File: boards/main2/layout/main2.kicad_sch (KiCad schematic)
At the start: 25 parts, among them IC1 STM32H725RGV6

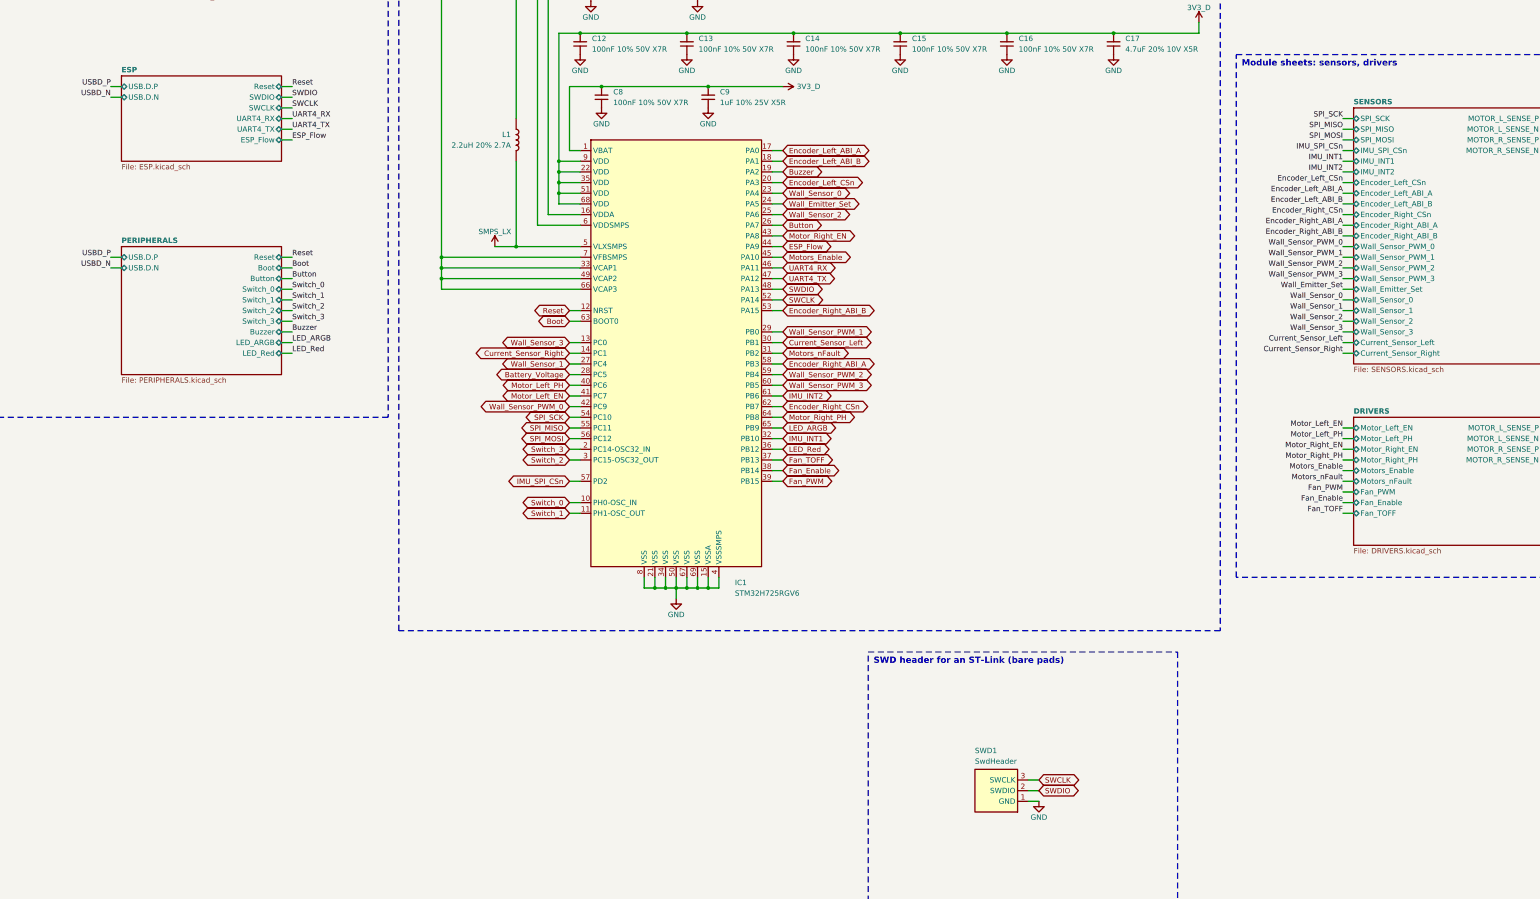
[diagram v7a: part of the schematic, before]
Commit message: 🚧 Swap main2's USB and ESP32-S3 for an ESP32-C5 and programming headers
Schematic and component checkpoint; the layout follows in its own commit.

- Remove USB-C, its ESD, power path and VBUS sense; both MCUs flash over
  the air.
- U13 ESP32-C5-MINI-1-N4 (dual-band, 5 GHz channels 36-48) in the
  rear-right corner, with its antenna notch on the right edge. SW4 and its
  notch move to the rear-left.
- H7-C5 link: SPI2 half-duplex 3-wire (PA12 SCK, PA11 CSn, PB14 DATA with
  IOSWP), PA9 flow control, UART4 fallback on the same pins. Fan_Enable
  moves to PB10, IMU INT1 to PB6, INT2 is left open.
- J2: 2x3 1.27 mm header in the ESP-Prog layout. SWD1: 1x4 1.27 mm in
  clone ST-Link order (SWDIO, GND, SWCLK, 5V). 5V_IN feeds VSYS through
  D17 (B5819W) to flash without the battery.
- R44/R45 to 20k/2k keeps PC5 below its absolute maximum at the clamp.
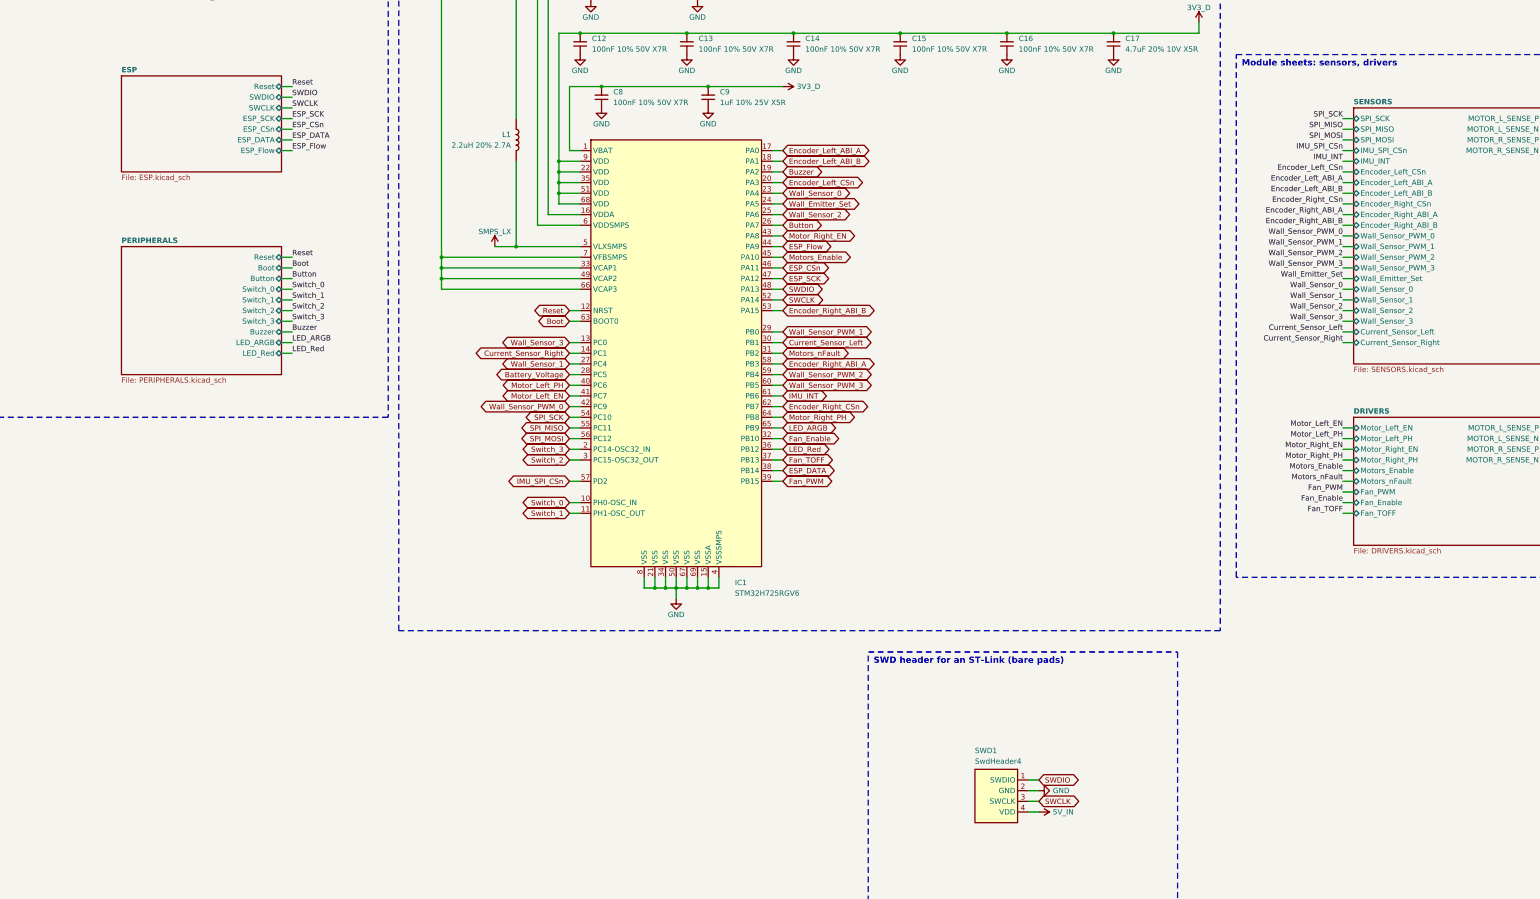
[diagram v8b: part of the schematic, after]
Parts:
- SWD1: value SwdHeader -> SwdHeader4; footprint Team-Micras_MicrasPCB_components_micras_SwdHeader:PinHeader_1x03_P1.27mm_Vertical -> Team-Micras_MicrasPCB_components_micras_SwdHeader:PinHeader_1x04_P1.27mm_Vertical; symbol SwdHeader -> SwdHeader4
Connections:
- net IMU_INT1 is gone; now on net Fan_Enable: IC1.32 (PB10)
- net Fan_Enable: no longer IC1.38 (PB14)
- net GND: now also SWD1.2 (GND); no longer SWD1.1 (GND)
- net SWDIO: now also SWD1.1 (SWDIO); no longer SWD1.2 (SWDIO)
- net IMU_INT2 renamed IMU_INT
- net UART4_RX renamed ESP_CSn
- net UART4_TX renamed ESP_SCK
- new net 5V_IN: SWD1.4 (VDD)
- new net ESP_DATA: IC1.38 (PB14)
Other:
- sheet ESP ports: added ESP_CSn, ESP_DATA, ESP_SCK; removed UART4_RX, UART4_TX, USB.D.N, USB.D.P
- sheet PERIPHERALS ports: added none; removed USB.D.N, USB.D.P
- sheet SENSORS ports: added IMU_INT; removed IMU_INT1, IMU_INT2
